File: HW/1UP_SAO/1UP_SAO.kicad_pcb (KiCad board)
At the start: 2 copper layers, 48 x 48 mm, 16 parts, among them X1 Badgelife_sao_connector_v169b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

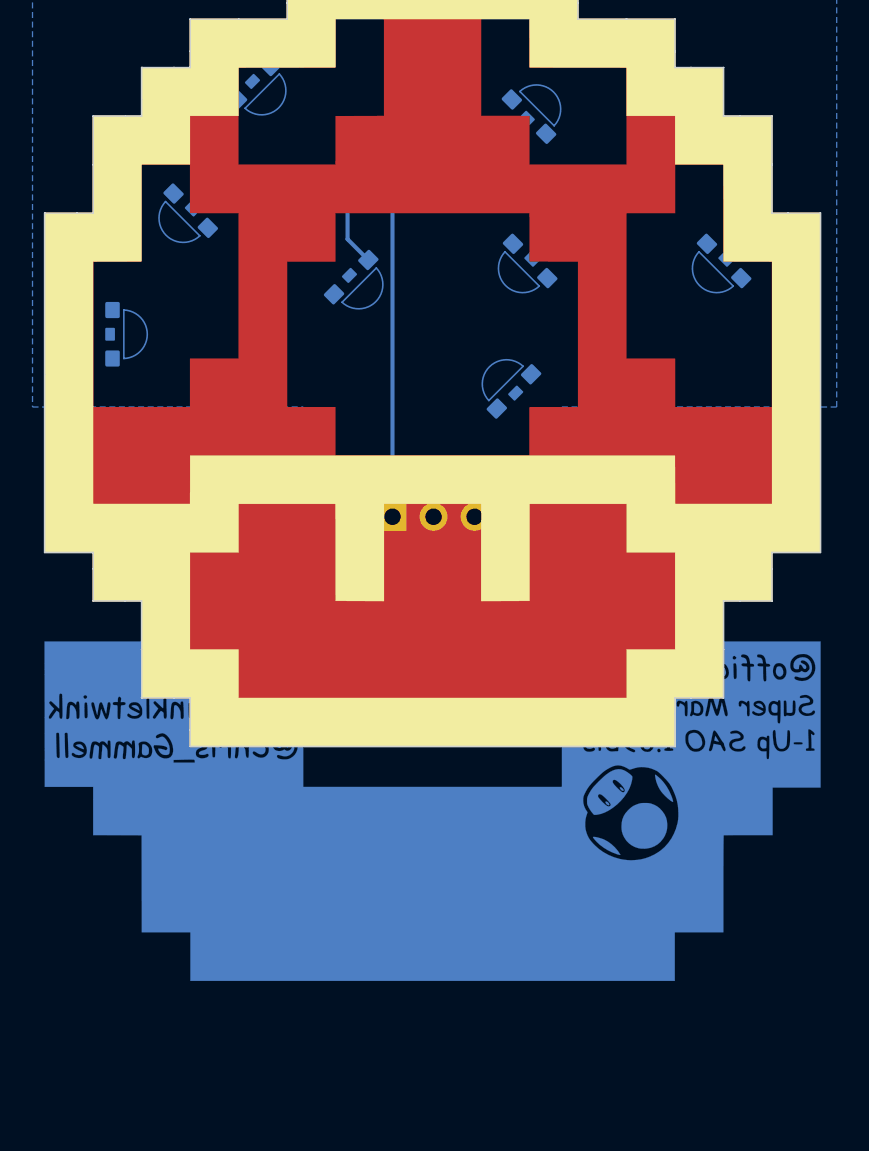
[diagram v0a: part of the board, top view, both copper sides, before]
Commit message: adding keepout and B.mask to center dot. Routing
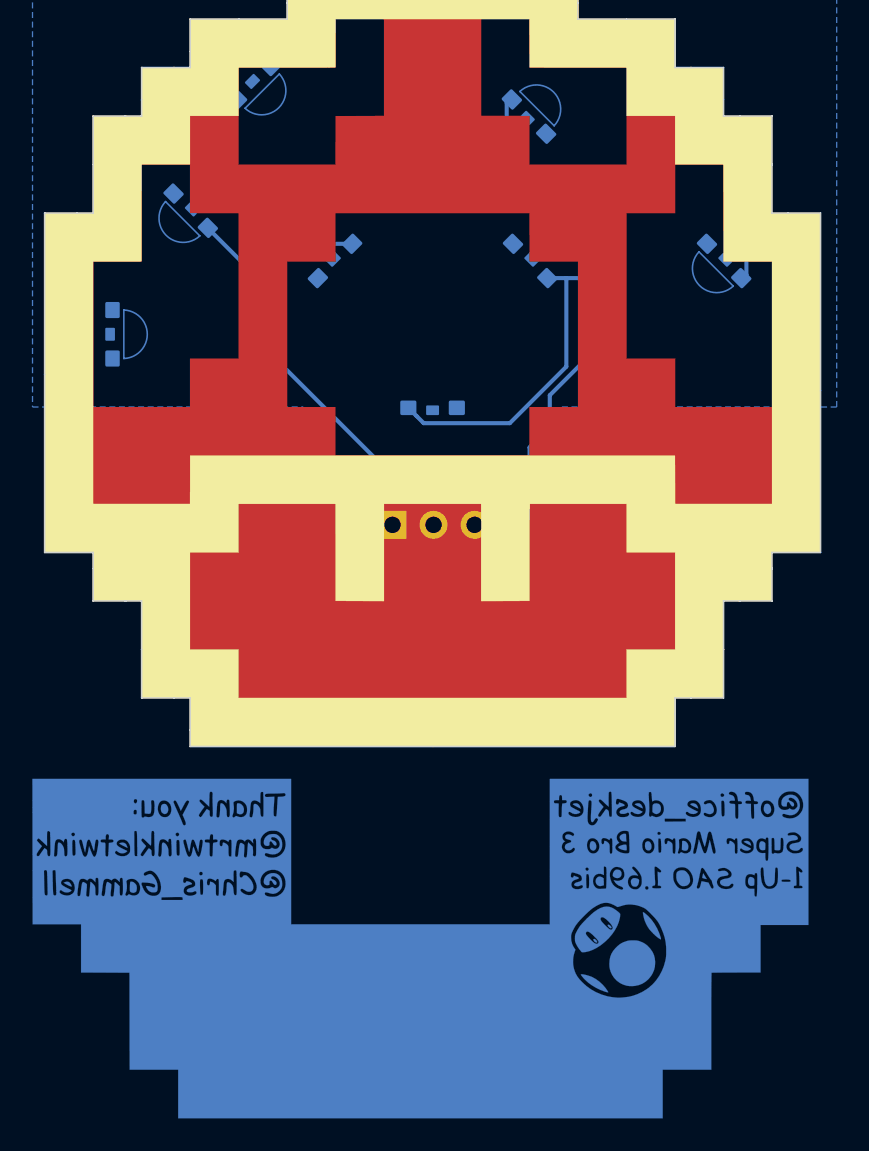
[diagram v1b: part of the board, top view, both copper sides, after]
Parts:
- removed De: LED, 1UP_SAO:1204_SIDE_VIEW_LED_TRANSPARENT
- removed the G*** at (100.0, 100.0) (x3)
- removed the G*** at (100.0, 114.5)
- added D8: LED, 1UP_SAO:1204_SIDE_VIEW_LED_TRANSPARENT, B.Cu at (100.0, 103.0)
- added G***: F.Mask, LOGO, F.Cu at (100.0, 100.0)
- added G***: B.Silk, LOGO, F.Cu at (100.0, 100.0)
- added G***: B.Cu, LOGO, F.Cu at (99.2, 123.0)
- added G***: LOGO, LOGO, F.Cu at (100.0, 100.0)
- moved R2 12.2 mm to (110.5, 98.0)
- moved R1 12.0 mm to (89.5, 98.0)
- moved D2 1.41 mm to (94.0, 94.0)
- moved X1 0.50 mm to (100.0, 109.0)
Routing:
- net Net-(D5-Pad2): track 0.00 -> 54.1 mm
- net VCC: track 22.0 -> 32.6 mm
- net Net-(D1-Pad2): track 9.03 -> 12.9 mm

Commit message: Fixed Vcc Gnd short on F.Cu layer.
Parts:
- removed the G*** at (99.2, 123.0)
- removed the G*** at (100.0, 100.0) (x2)
- added G***: LOGO, 1UP_SAO:F.Cu_cutout, F.Cu at (100.0, 100.0)
- added G***: B.Cu, LOGO, F.Cu at (100.0, 100.0)
- added G***: LOGO, LOGO, F.Cu at (100.0, 100.0)
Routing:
- net Net-(D1-Pad2): track 12.9 -> 42.9 mm
- added copper zone on F.Cu, net GND

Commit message: Need to change LED layout. Updated LED Footprint
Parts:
- D1, D2, D3, D4, D5, D6, D7, D8: footprint 1UP_SAO:1204_SIDE_VIEW_LED_TRANSPARENT -> 1UP_SAO:1204_SIDE_VIEW_LED
- moved G*** 61.9 mm to (40.0, 84.8)

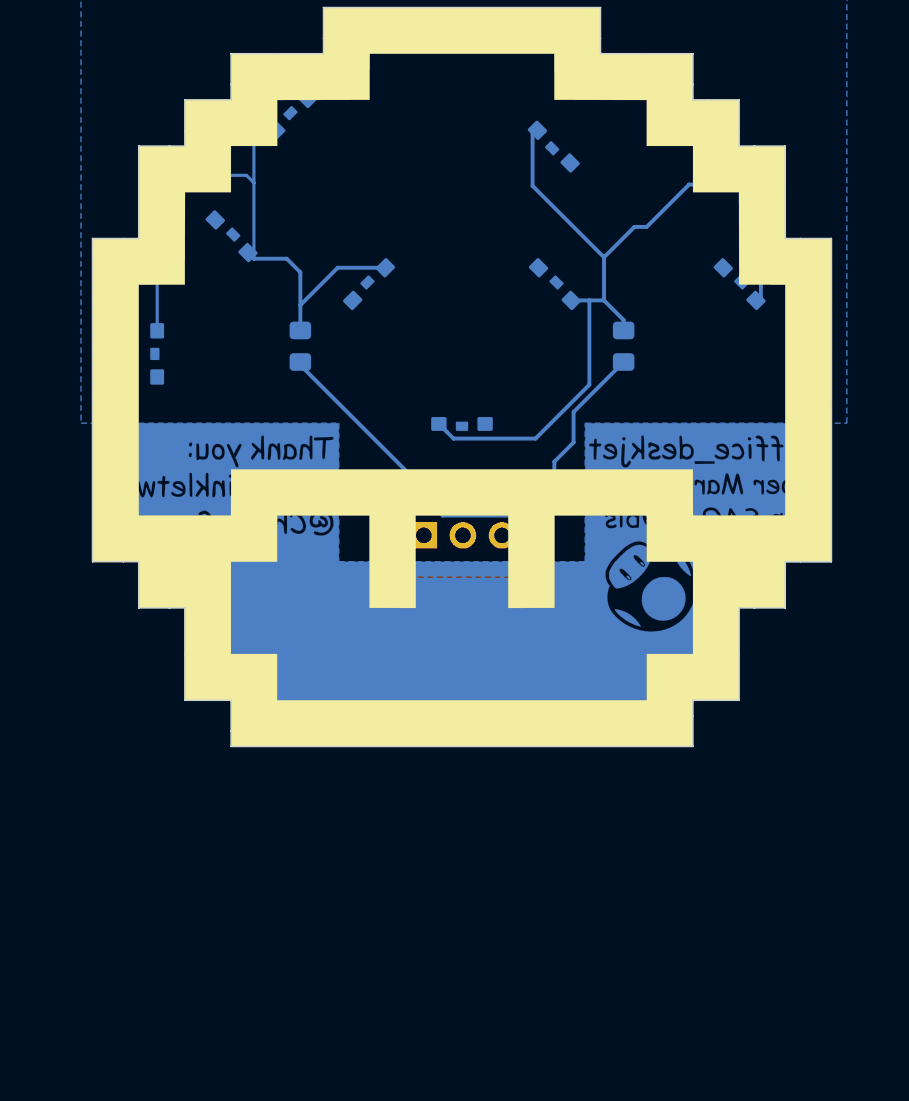
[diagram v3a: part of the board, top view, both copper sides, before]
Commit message: adding footprint for B.Mask to let light through.
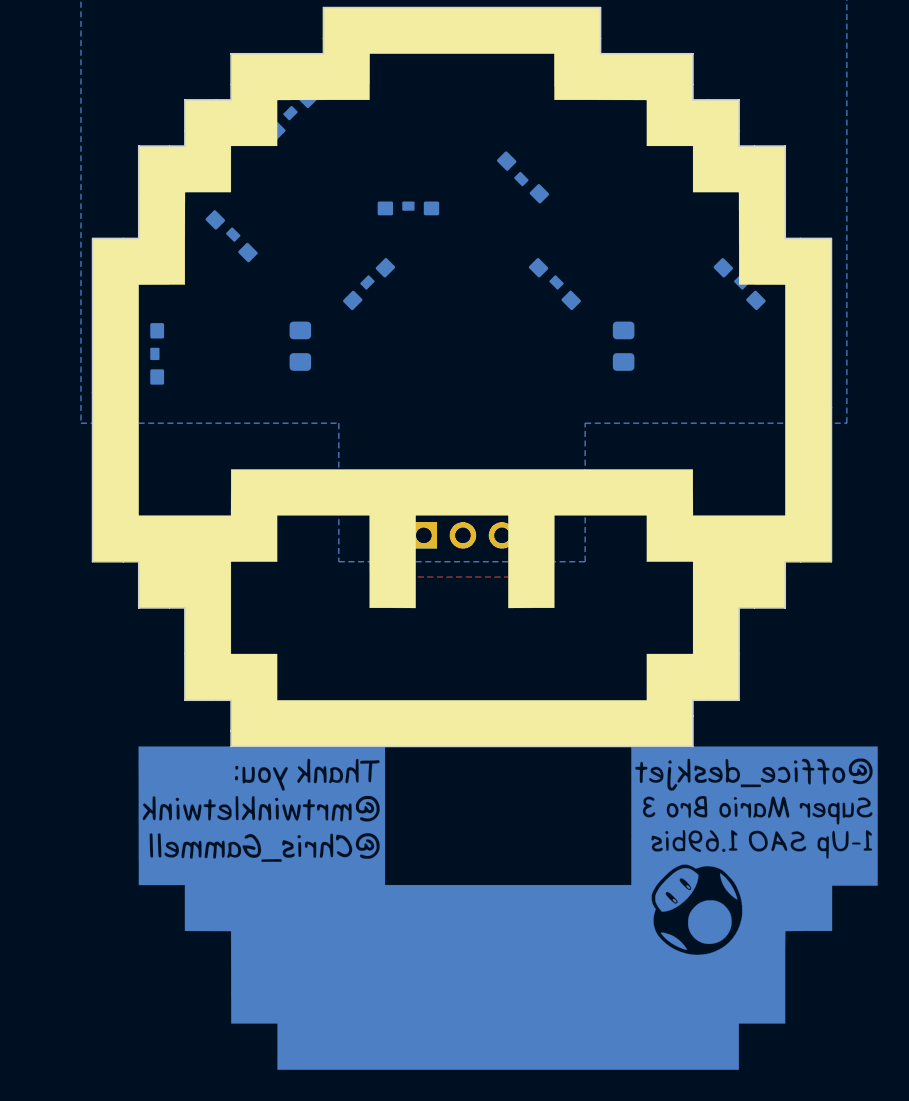
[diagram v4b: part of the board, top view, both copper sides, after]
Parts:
- added B.Mask: LOGO, 1UP_SAO:B.Mask_g4150, F.Cu at (100.0, 100.0)
- moved G*** 21.2 mm to (103.0, 121.0)
- moved D8 14.3 mm to (96.5, 89.1), turned to 0 degrees
- moved D5 2.83 mm to (104.0, 87.0)
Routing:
- net Net-(D5-Pad2): track 54.1 -> 0.00 mm
- net Net-(D1-Pad2): track 42.9 -> 0.00 mm
- net VCC: track 32.6 -> 0.00 mm

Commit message: placed top LEDS
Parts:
- moved G*** 22.6 mm to (119.0, 137.0)
- moved D1 3.40 mm to (86.2, 85.0), turned to 90 degrees
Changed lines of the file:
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@@
     (46 B.CrtYd user)
     (47 F.CrtYd user hide)
-    (48 B.Fab user)
+    (48 B.Fab user hide)
     (49 F.Fab user hide)
   )
   (setup
-    (last_trace_width 0.2032)
+    (last_trace_width 0.254)
     (user_trace_width 0.2032)
     (user_trace_width 0.2286)
@@
     (add_net VCC)
   )
+  (module 1UP_SAO:B.Mask_g4150 locked (layer F.Cu)
+    (at 100 100)
+    (fp_text reference B.Mask (at 0 0) (layer F.SilkS) hide
+      (effects (font (size 1.524 1.524) (thickness 0.3)))
+    )
+    (fp_text value LOGO (at 0.75 0) (layer F.SilkS) hide
+      (effects (font (size 1.524 1.524) (thickness 0.3)))
+    )
+    (fp_poly (pts (xy 6.00075 -18.00225) (xy 12.0015 -17.991522) (xy 12.0015 -12.0015) (xy 6.011617 -12.0015)
+      (xy 6.006183 -13.499042) (xy 6.00075 -14.996584) (xy 4.503208 -15.002017) (xy 3.005666 -15.007451)
+      (xy 3.005666 -20.997334) (xy 5.989882 -20.997334) (xy 6.00075 -18.00225)) (layer B.Mask) (width 0.01))
+    (fp_poly (pts (xy -3.005667 -15.007451) (xy -4.503209 -15.002017) (xy -6.00075 -14.996584) (xy -6.011618 -12.0015)
+      (xy -12.0015 -12.0015) (xy -12.0015 -17.991522) (xy -6.00075 -18.00225) (xy -5.995317 -19.499792)
+      (xy -5.989883 -20.997334) (xy -3.005667 -20.997334) (xy -3.005667 -15.007451)) (layer B.Mask) (width 0.01))
+    (fp_poly (pts (xy 17.996885 -9.001125) (xy 18.00225 -6.00075) (xy 19.499791 -5.995317) (xy 20.997333 -5.989883)
+      (xy 20.997333 3.005666) (xy 15.007166 3.005666) (xy 15.007166 0) (xy 12.0015 0)
+      (xy 12.0015 -8.995834) (xy 15.007166 -8.995834) (xy 15.007166 -12.0015) (xy 16.499343 -12.0015)
+      (xy 17.991521 -12.001501) (xy 17.996885 -9.001125)) (layer B.Mask) (width 0.01))
+    (fp_poly (pts (xy -15.007167 -8.995834) (xy -12.0015 -8.995834) (xy -12.0015 0) (xy -15.007167 0)
+      (xy -15.007167 3.005666) (xy -20.997334 3.005666) (xy -20.997334 -5.989883) (xy -19.499792 -5.995317)
+      (xy -18.00225 -6.00075) (xy -17.991522 -12.0015) (xy -15.007167 -12.0015) (xy -15.007167 -8.995834)) (layer B.Mask) (width 0.01))
+    (fp_poly (pts (xy 6.00075 -6.00075) (xy 7.498291 -5.995317) (xy 8.995833 -5.989883) (xy 8.995833 1.989382)
+      (xy 7.498291 1.994816) (xy 6.00075 2.00025) (xy 5.995316 3.497791) (xy 5.989882 4.995333)
+      (xy -5.989883 4.995333) (xy -5.995317 3.497791) (xy -6.00075 2.00025) (xy -8.995834 1.989382)
+      (xy -8.995834 -5.989883) (xy -7.498292 -5.995317) (xy -6.00075 -6.00075) (xy -5.995317 -7.498292)
+      (xy -5.989883 -8.995834) (xy 5.989882 -8.995834) (xy 6.00075 -6.00075)) (layer B.Mask) (width 0.01))
+  )
   (module 1UP_SAO:Badgelife-SAOv169-SAO-2x3 (layer F.Cu)
     (at 100 109)
@@
     )
   )
-  (module 1UP_SAO:B.Mask_g4150 locked (layer F.Cu)
-    (at 100 100)
-    (fp_text reference B.Mask (at 0 0) (layer F.SilkS) hide
-      (effects (font (size 1.524 1.524) (thickness 0.3)))
-    )
-    (fp_text value LOGO (at 0.75 0) (layer F.SilkS) hide
-      (effects (font (size 1.524 1.524) (thickness 0.3)))
-    )
-    (fp_poly (pts (xy 6.00075 -18.00225) (xy 12.0015 -17.991522) (xy 12.0015 -12.0015) (xy 6.011617 -12.0015)
-      (xy 6.006183 -13.499042) (xy 6.00075 -14.996584) (xy 4.503208 -15.002017) (xy 3.005666 -15.007451)
-      (xy 3.005666 -20.997334) (xy 5.989882 -20.997334) (xy 6.00075 -18.00225)) (layer B.Mask) (width 0.01))
-    (fp_poly (pts (xy -3.005667 -15.007451) (xy -4.503209 -15.002017) (xy -6.00075 -14.996584) (xy -6.011618 -12.0015)
-      (xy -12.0015 -12.0015) (xy -12.0015 -17.991522) (xy -6.00075 -18.00225) (xy -5.995317 -19.499792)
-      (xy -5.989883 -20.997334) (xy -3.005667 -20.997334) (xy -3.005667 -15.007451)) (layer B.Mask) (width 0.01))
-    (fp_poly (pts (xy 17.996885 -9.001125) (xy 18.00225 -6.00075) (xy 19.499791 -5.995317) (xy 20.997333 -5.989883)
-      (xy 20.997333 3.005666) (xy 15.007166 3.005666) (xy 15.007166 0) (xy 12.0015 0)
-      (xy 12.0015 -8.995834) (xy 15.007166 -8.995834) (xy 15.007166 -12.0015) (xy 16.499343 -12.0015)
-      (xy 17.991521 -12.001501) (xy 17.996885 -9.001125)) (layer B.Mask) (width 0.01))
-    (fp_poly (pts (xy 6.00075 -6.00075) (xy 7.498291 -5.995317) (xy 8.995833 -5.989883) (xy 8.995833 3.005666)
-      (xy -8.995834 3.005666) (xy -8.995834 -5.989883) (xy -7.498292 -5.995317) (xy -6.00075 -6.00075)
-      (xy -5.995317 -7.498292) (xy -5.989883 -8.995834) (xy 5.989882 -8.995834) (xy 6.00075 -6.00075)) (layer B.Mask) (width 0.01))
-    (fp_poly (pts (xy -15.007167 -8.995834) (xy -12.0015 -8.995834) (xy -12.0015 0) (xy -15.007167 0)
-      (xy -15.007167 3.005666) (xy -20.997334 3.005666) (xy -20.997334 -5.989883) (xy -19.499792 -5.995317)
-      (xy -18.00225 -6.00075) (xy -17.991522 -12.0015) (xy -15.007167 -12.0015) (xy -15.007167 -8.995834)) (layer B.Mask) (width 0.01))
-  )
   (module 1UP_SAO:1204_SIDE_VIEW_LED (layer B.Cu)
     (at 80.25 98.5 90)
@@
   )
   (module 1UP_SAO:1204_SIDE_VIEW_LED (layer B.Cu)
-    (at 89 83 45)
-    (fp_text reference D1 (at -3.1 0 315) (layer B.SilkS)
+    (at 86.25 85 90)
+    (fp_text reference D1 (at -3.1 0 180) (layer B.SilkS)
       (effects (font (size 0.7 0.7) (thickness 0.15)) (justify mirror))
     )
-    (fp_text value LED (at 0 4.199999 45) (layer B.Fab)
+    (fp_text value LED (at 0 4.199999 90) (layer B.Fab)
       (effects (font (size 1 1) (thickness 0.15)) (justify mirror))
     )
@@
     (fp_line (start 0.3 -1.25) (end 0.3 -1.85) (layer B.SilkS) (width 0.15))
     (fp_arc (start 0 0.4) (end 1 0.4) (angle 180) (layer B.SilkS) (width 0.15))
-    (pad "" smd roundrect (at 0 -0.2 45) (size 0.8 0.6) (layers B.Cu B.Paste B.Mask) (roundrect_rratio 0.1))
-    (pad 2 smd roundrect (at 1.5 -0.05 45) (size 1 0.9) (layers B.Cu B.Paste B.Mask) (roundrect_rratio 0.1)
+    (pad "" smd roundrect (at 0 -0.2 90) (size 0.8 0.6) (layers B.Cu B.Paste B.Mask) (roundrect_rratio 0.1))
+    (pad 2 smd roundrect (at 1.5 -0.05 90) (size 1 0.9) (layers B.Cu B.Paste B.Mask) (roundrect_rratio 0.1)
       (net 1 "Net-(D1-Pad2)"))
-    (pad 1 smd roundrect (at -1.5 -0.05 45) (size 1 0.9) (layers B.Cu B.Paste B.Mask) (roundrect_rratio 0.1)
+    (pad 1 smd roundrect (at -1.5 -0.05 90) (size 1 0.9) (layers B.Cu B.Paste B.Mask) (roundrect_rratio 0.1)
       (net 2 GND))
   )
@@
       (xy 3.005666 -20.997334) (xy 5.989882 -20.997334) (xy 6.00075 -18.00225)) (layer F.Mask) (width 0.01))
   )
-  (module LOGO locked (layer F.Cu)
+  (module LOGO (layer F.Cu)
     (at 100 100)
     (fp_text reference G*** (at 0 0) (layer F.SilkS) hide
@@
   )
   (module LOGO (layer F.Cu)
-    (at 103 121)
+    (at 119 137)
     (fp_text reference G*** (at 0 0) (layer F.SilkS) hide
       (effects (font (size 1.524 1.524) (thickness 0.3)))
@@
       (xy 8.995833 -24.003) (xy 8.995833 -20.997334)) (layer F.SilkS) (width 0.01))
   )
-  (gr_circle (center 71.962 70.358) (end 76.962 70.358) (layer B.SilkS) (width 0.15))
+  (gr_circle (center 62.5 80.75) (end 67.5 80.75) (layer B.SilkS) (width 0.15))
   (gr_line (start 85 123) (end 85 121) (layer Edge.Cuts) (width 0.1))
   (gr_line (start 85 121) (end 84 121) (layer Edge.Cuts) (width 0.1))
@@
     (polygon
       (pts
-        (xy 109 94) (xy 106 94) (xy 106 91) (xy 94 91) (xy 94 94)
-        (xy 91 94) (xy 91 103) (xy 109 103)
+        (xy 106 91) (xy 94 91) (xy 94 94) (xy 91 94) (xy 91 102)
+        (xy 94 102) (xy 94 105) (xy 106 105) (xy 106 102) (xy 109 102)
+        (xy 109 94) (xy 106 94)
       )
     )
